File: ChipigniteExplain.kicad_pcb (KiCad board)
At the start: 4 copper layers, 53.5 x 65.5 mm, 251 parts, among them J1 Conn_01x02, J10 Conn_01x02, J11 Conn_01x06, J2 Conn_01x02, J3 Conn_01x03, J4 USB_C, J5 613012243121, J6 613012243121, J7 Conn_02x03_Odd_Even, Q1 DMN2005K, SW1 434121025816, SW2 434121025816, SW3 434121025816, SW4 434121025816, SW5 434121025816, SW6 193-8MSR, U1 TLV1117LV33, U2 TPD1E05U06QDPYRQ1, U3 157112V12700, U4 RP2040, U5 W25Q32JVSS, U6 AP2112K-1.2, U7 ICE40UP5K-SG48ITR, X1 24MHz, Y1 12.0MHz

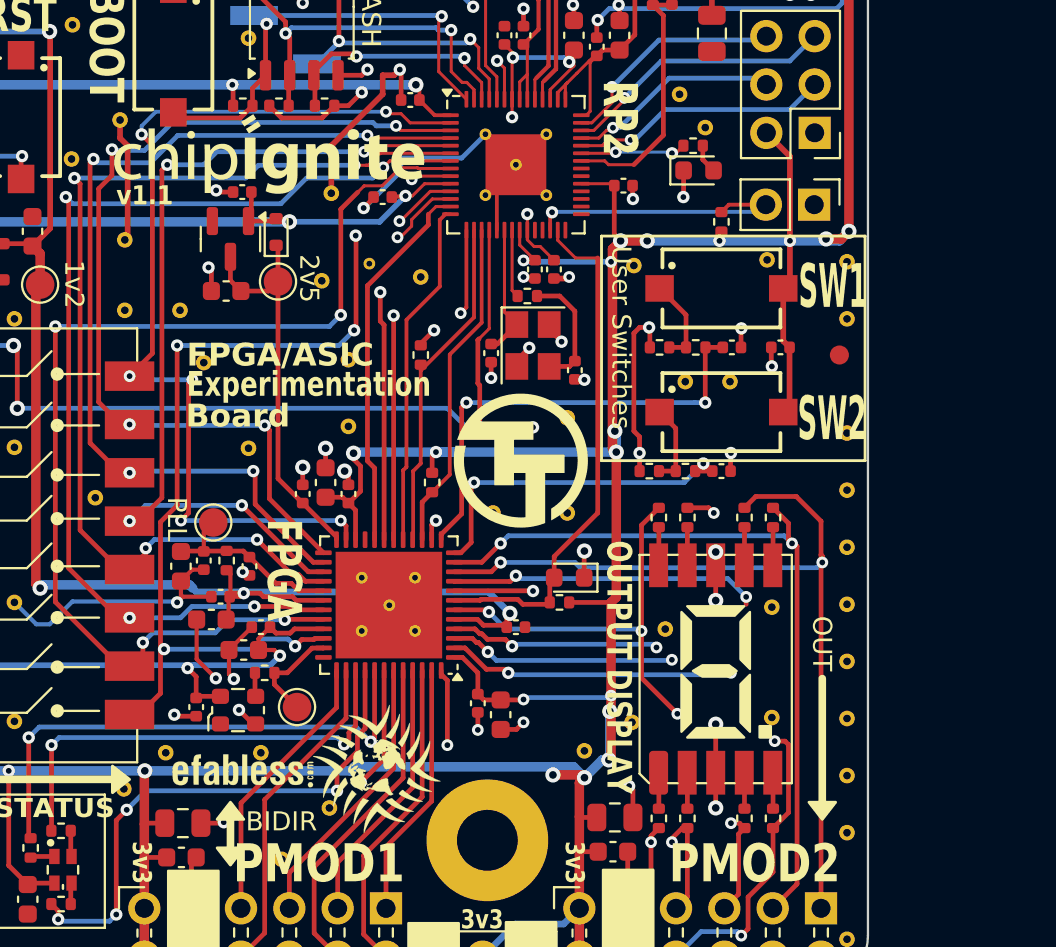
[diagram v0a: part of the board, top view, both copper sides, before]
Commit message: revised to remove EF branding, adjust LED resistors, and invert SW2 button for reset.
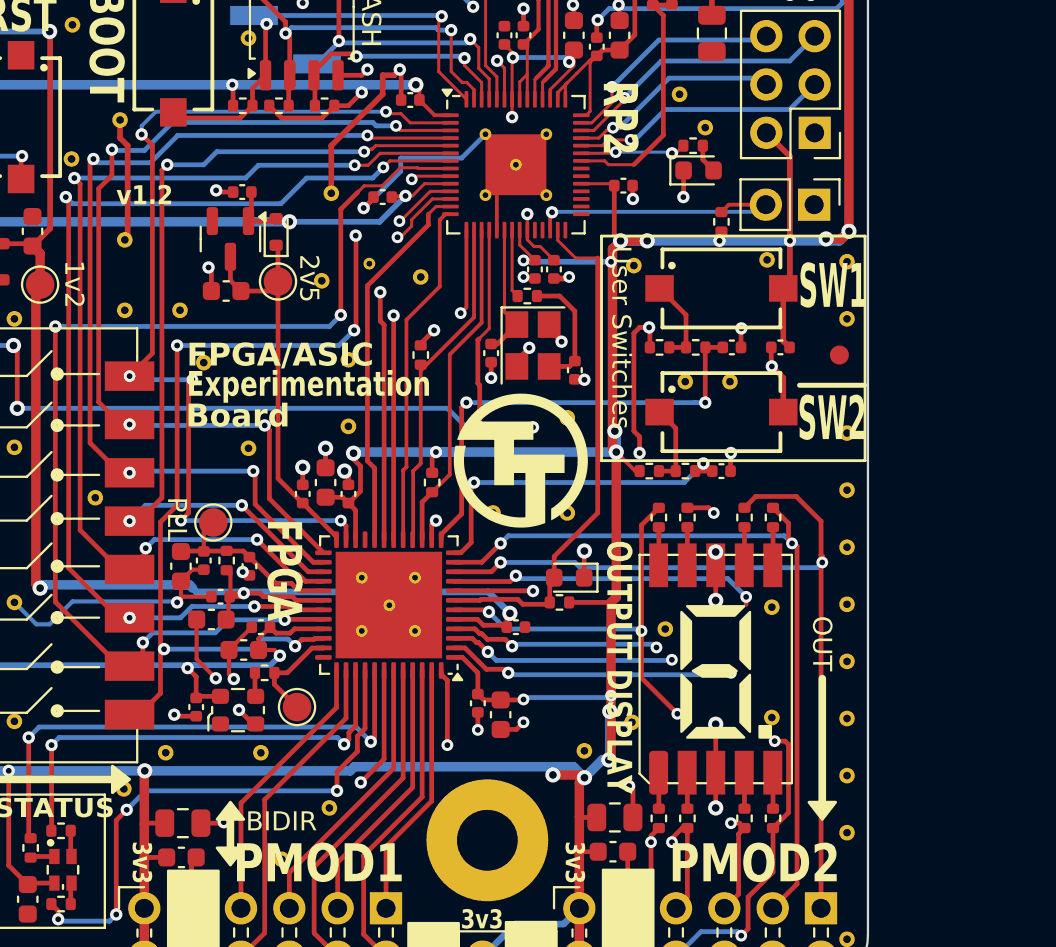
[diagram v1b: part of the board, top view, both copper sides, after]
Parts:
- removed EFABLOG: Logo, Logo:ef_logo_graphical
- removed EFABTXT (x2): Logo, Logo:ef_logo
- removed REF**: chipignite_logo_med, Logo:chipignite_logo_med
- removed REF**: chipignite_logo, Logo:chipignite_logo
- R42, R43, R44, R45, R46, R47, R48, R49: value 510R -> 68R
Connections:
- R23 pad 2: GND -> +3V3
- SW4 pad 2: +3V3 -> GND
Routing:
- net GND: track 204.1 -> 206.3 mm
- net +3V3: track 459.5 -> 457.6 mm
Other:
- board text added: "v1.2"
- board text added: "~{SW2}"
- board text removed: "Designed for"
- board text removed: "SW2"
- board text removed: "efabless.com/chipignite"
- board text removed: "v1.1"
